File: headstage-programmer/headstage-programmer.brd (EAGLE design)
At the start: 22 x 49 mm, 19 parts, among them U1 TPS61202

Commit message: Minor change to headstage-programmer.
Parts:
- moved TP1 3.50 mm to (7.25, 27.8)
- moved TP2 3.50 mm to (3.75, 27.8)
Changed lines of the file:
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@@
 <wire x1="5" y1="49" x2="0" y2="44" width="0" layer="20"/>
 <wire x1="0" y1="44" x2="0" y2="0" width="0" layer="20"/>
-<text x="8" y="28.5" size="1.27" layer="21" font="vector" ratio="17" align="center-right">VCOAX</text>
-<text x="2.25" y="26.75" size="1.27" layer="21" font="vector" ratio="17" rot="R180" align="center-right">GND</text>
-<wire x1="3.75" y1="25.75" x2="3.75" y2="25.25" width="0.254" layer="21"/>
-<wire x1="7.25" y1="26.25" x2="6.75" y2="27.5" width="0.254" layer="21"/>
+<text x="7.25" y="26.75" size="1.27" layer="21" font="vector" ratio="17" rot="R90" align="center-right">VCOAX</text>
+<text x="3.75" y="26.75" size="1.27" layer="21" font="vector" ratio="17" rot="R90" align="center-right">GND</text>
 <wire x1="18.75" y1="18" x2="14" y2="18" width="0.254" layer="21"/>
-<wire x1="7.25" y1="26.25" x2="7.25" y2="25.5" width="0.254" layer="21"/>
 <text x="2" y="17.25" size="1.27" layer="21" font="vector" ratio="17" rot="R270" align="center-right">2.2uH</text>
 <wire x1="5" y1="45" x2="7.75" y2="46.75" width="0.254" layer="21"/>
@@
 <attribute name="VALUE" x="10.96" y="44.71" size="1.016" layer="27" font="vector" ratio="18"/>
 </element>
-<element name="TP1" library="jonnew" package="TESTPOINT_1MM" value="" x="7.25" y="24.25" smashed="yes">
-<attribute name="VALUE" x="8.266" y="23.7674" size="0.8128" layer="27" font="vector" ratio="18"/>
-</element>
-<element name="TP2" library="jonnew" package="TESTPOINT_1MM" value="" x="3.75" y="24.25" smashed="yes">
-<attribute name="VALUE" x="4.766" y="23.7674" size="0.8128" layer="27" font="vector" ratio="18"/>
+<element name="TP1" library="jonnew" package="TESTPOINT_1MM" value="" x="7.25" y="27.75" smashed="yes">
+<attribute name="VALUE" x="8.266" y="27.2674" size="0.8128" layer="27" font="vector" ratio="18"/>
+</element>
+<element name="TP2" library="jonnew" package="TESTPOINT_1MM" value="" x="3.75" y="27.75" smashed="yes">
+<attribute name="VALUE" x="4.766" y="27.2674" size="0.8128" layer="27" font="vector" ratio="18"/>
 </element>
 <element name="R1" library="jonnew" package="0603" value="2k" x="1.75" y="42" smashed="yes" rot="R270">

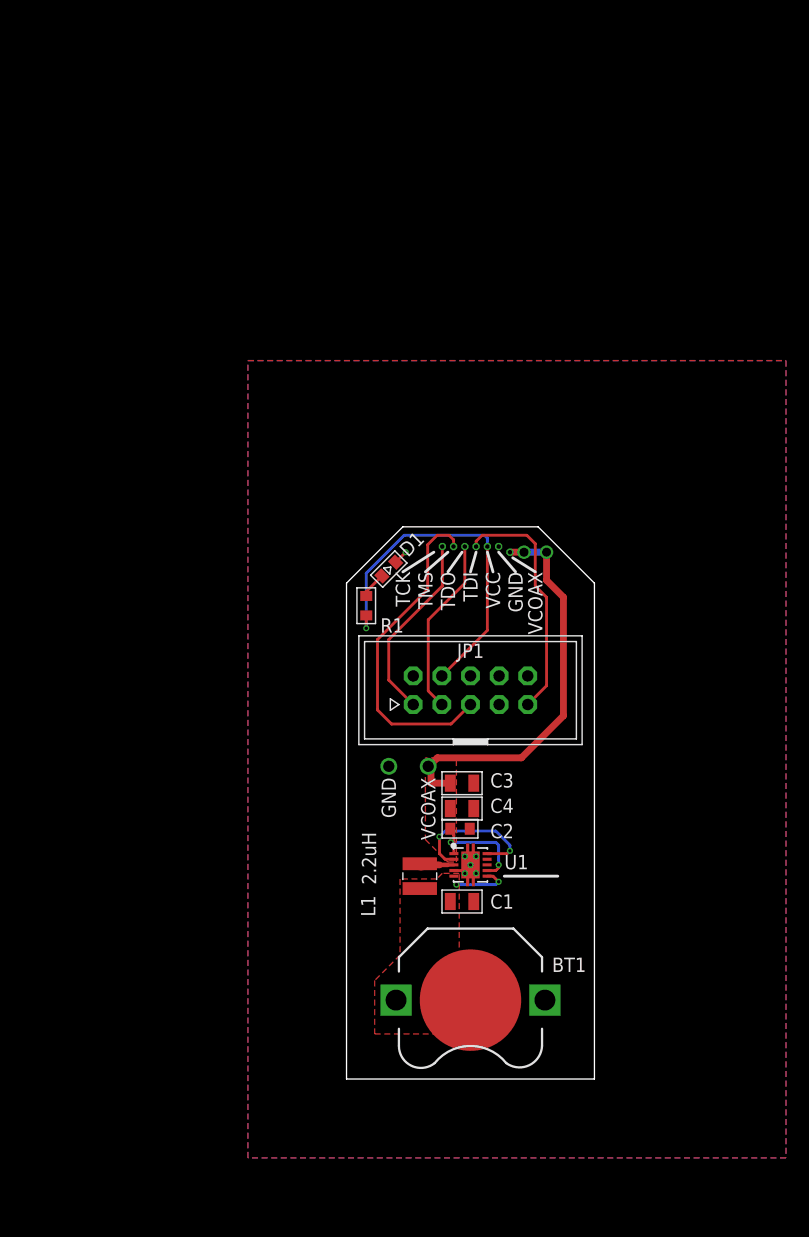
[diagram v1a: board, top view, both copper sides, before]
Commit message: Headstage programmer modifications
- Due to discussions with Jakob
- Coin cell replaced with AAA battery
- Orientation of programming pins rotated
- JTAG connector removed to rear
- Reverse polarity protection in case coax is plugged in during
programming
- Power switch
- Flashlight LED on bottom
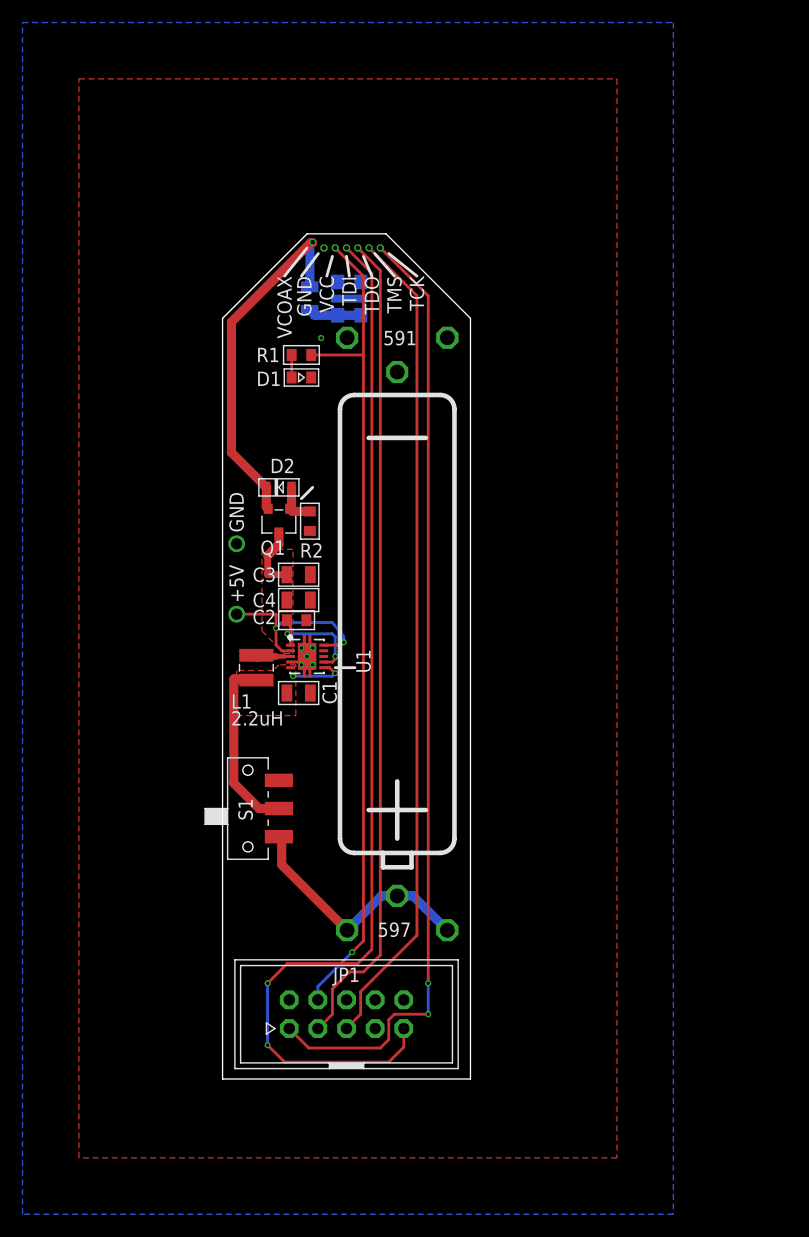
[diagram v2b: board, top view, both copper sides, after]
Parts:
- removed BT1: (no value), SparkFun-Batteries:BATTCON_12MM_PTH
- added D2: UDZ10B-7, jonnew:SOD-323
- added D3: MLEAWT-A1, jonnew:LED-MLE
- added Q1: DMP3056L, jonnew:SOT23-GSD
- added R2: 1k, jonnew:0603
- added R3: 220, jonnew:0805
- added S1: (no value), jonnew:JS102011SAQN
- added U2: (no value), jonnew:597/591_AAA-HOLDER
- moved VCOAX 32.6 mm to (-3.00, 74.2), turned to 180 degrees
- moved JP1 30.8 mm to (0.00, 5.75)
- moved GND 30.7 mm to (-2.00, 73.8), turned to 180 degrees
- moved VCC 29.7 mm to (-1.00, 73.8), turned to 180 degrees
- moved TDI 28.9 mm to (0.00, 73.8), turned to 180 degrees
- moved TDO 28.2 mm to (1.00, 73.8), turned to 180 degrees
- moved TMS 27.5 mm to (2.00, 73.8), turned to 180 degrees
- moved TCK 27.1 mm to (3.00, 73.8), turned to 180 degrees
- moved TP2 23.9 mm to (-9.75, 47.5)
- moved C1 23.5 mm to (-4.25, 34.2)
- moved C2 23.5 mm to (-4.43, 40.7)
- moved C3 23.5 mm to (-4.25, 44.8)
- moved C4 23.5 mm to (-4.25, 42.5)
- moved L1 23.5 mm to (-8.00, 36.5)
- moved U1 23.5 mm to (-3.50, 37.5)
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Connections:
- new net N$2: D3.A1, D3.A2, R3.1
- new net N$4: S1.3, U2.+1, U2.+2, U2.+3
- new net N$450: D2.A, Q1.G, R2.2
- new net VO: C3.1, C4.1, Q1.D, TP1.1, U1.10, U1.2
- net GND: now also D3.C1, D3.C2, D3.HS, R2.1, U2.-1, U2.-2, U2.-3; no longer BT1.GND
- net VCOAX: now also D2.C, Q1.S, R3.2; no longer C3.1, C4.1, TP1.1, U1.10, U1.2
- net VIN: now also S1.2; no longer BT1.VCC@1
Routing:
- net TDI: track 21.6 -> 94.1 mm, vias 0 -> 2
- net TCK: track 16.9 -> 85.1 mm, vias 0 -> 2
- net TDO: track 15.9 -> 73.1 mm
- net TMS: track 29.4 -> 73.6 mm
- net VCC(TRGT): track 32.2 -> 74.1 mm
- net VO: track 0.00 -> 22.8 mm, vias 0 -> 2
- net N$4: track 0.00 -> 22.4 mm
- net VIN: track 5.09 -> 21.4 mm
- net VCOAX: track 47.9 -> 32.3 mm, vias 4 -> 0
- net N$2: track 0.00 -> 4.70 mm
- net N$450: track 0.00 -> 3.87 mm
- net GND: track 2.34 -> 1.08 mm
- added copper zone on layer 1, net VO
- removed copper zone on layer 1, net VCOAX
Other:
- board size 22 x 49 mm -> 22 x 75 mm
- board text added: "+5V"
- board text added: "591"
- board text added: "597"
- board text removed: "VCOAX"

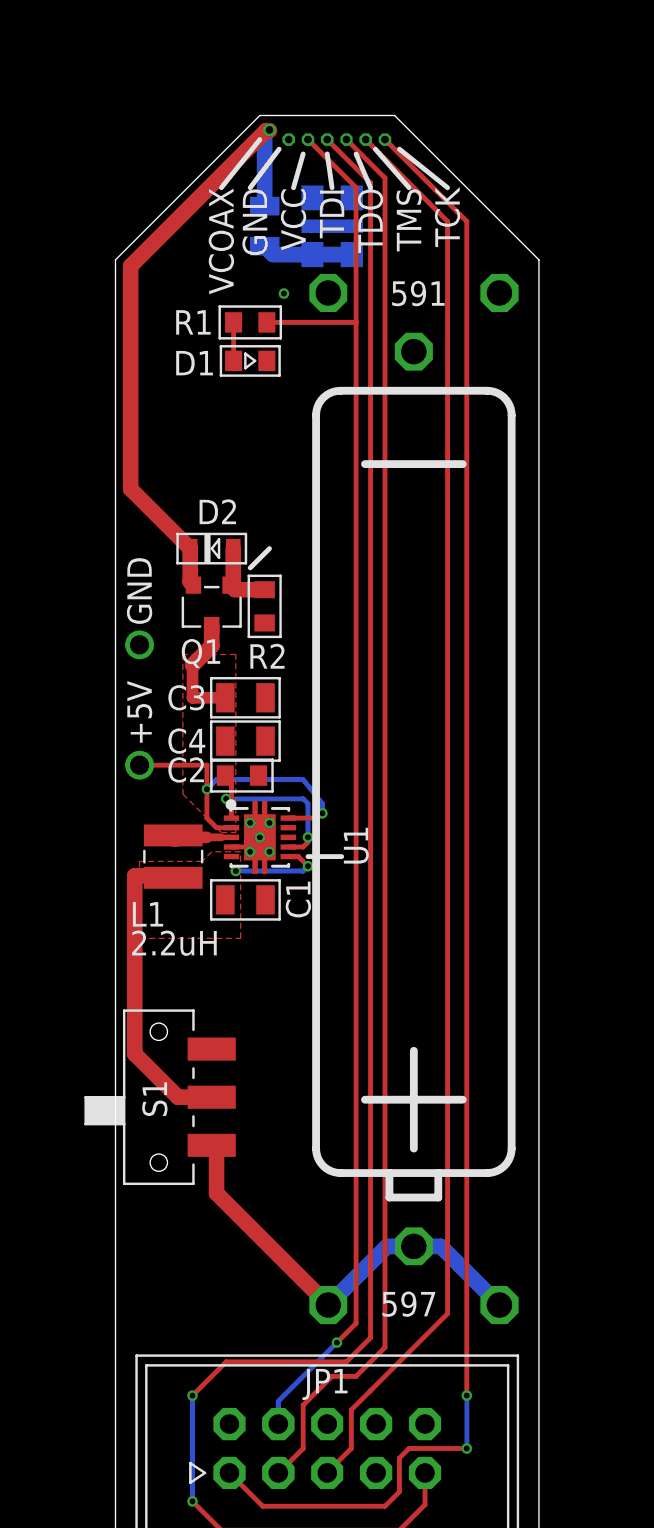
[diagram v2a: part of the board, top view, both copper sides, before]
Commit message: Changes to pogo JTAG programming dimensions
- Pins are now separated by 0.05 inches so that standard pins might be
possible to use
- There is not much clearance on the headstage-64 so we may still have
to use tiny pogo pins
- Fixed JTAG connectivity on headstage-64 by connecting +3V3 to
VCC(TRGT) pad
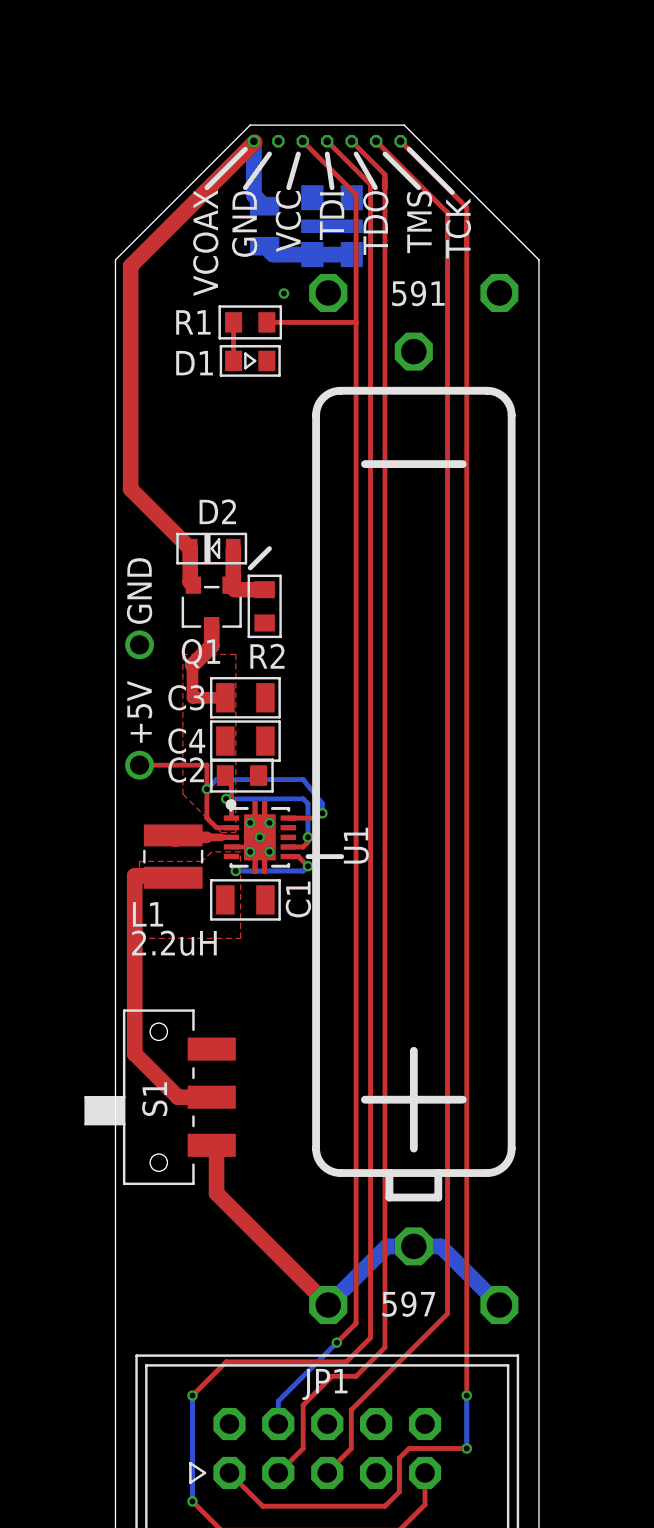
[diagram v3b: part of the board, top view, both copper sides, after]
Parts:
- moved VCOAX 1.00 mm to (-3.81, 73.7)
- moved TCK 0.81 mm to (3.81, 73.7)
- moved GND 0.55 mm to (-2.54, 73.7)
- moved TMS 0.55 mm to (2.54, 73.7)
- moved TDO 0.28 mm to (1.27, 73.7)
- moved VCC 0.28 mm to (-1.27, 73.7)
- moved TDI 0.09 mm to (0.00, 73.7)
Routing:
- net VCOAX: track 32.3 -> 30.7 mm
- net TCK: track 85.1 -> 85.9 mm
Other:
- board size 22 x 75 mm -> 22 x 74.5 mm

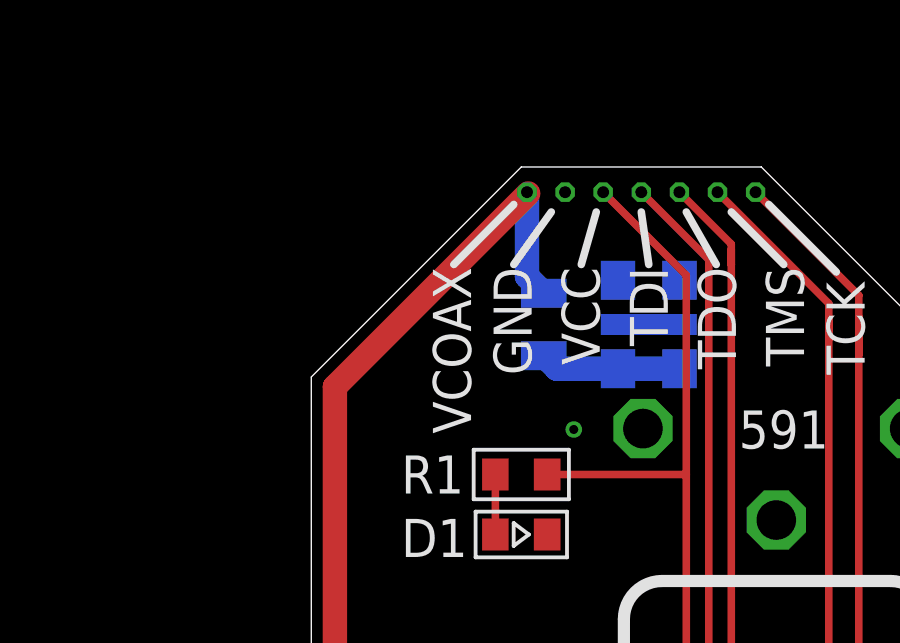
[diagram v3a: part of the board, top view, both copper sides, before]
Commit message: Headstage-64 routing refinements
- Update programmer to reflect switchee Vcoax/Gnd positions
- AGND/GND sprinkles for thermal and noise considerations
- Route optimization/simplificiation
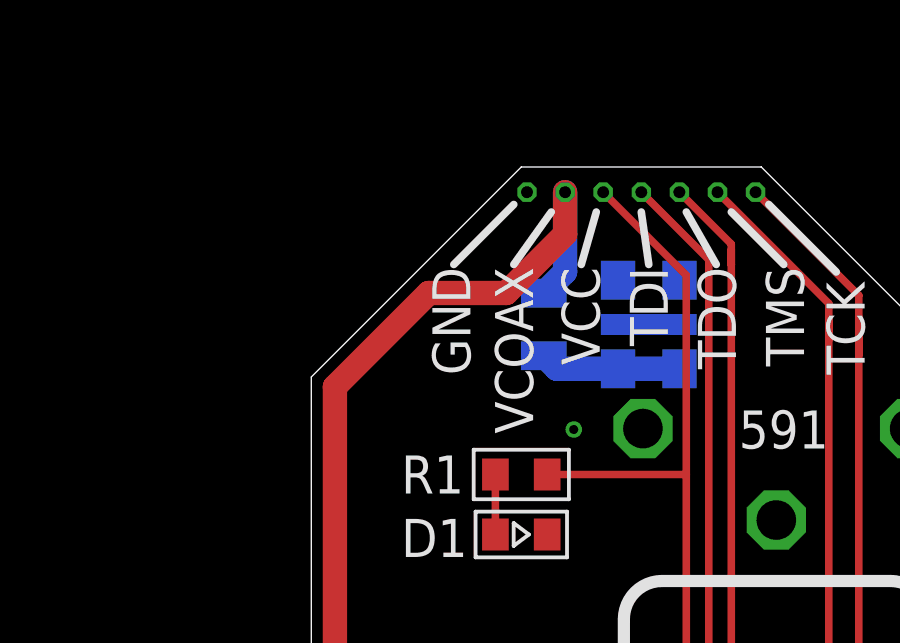
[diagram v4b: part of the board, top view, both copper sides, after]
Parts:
- moved GND 1.27 mm to (-3.81, 73.7)
- moved VCOAX 1.27 mm to (-2.54, 73.7)
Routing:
- net VCOAX: track 30.7 -> 32.8 mm
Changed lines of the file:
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@@
 <setting verticaltext="up"/>
 </settings>
-<grid distance="0.25" unitdist="mm" unit="mm" style="lines" multiple="1" display="yes" altdistance="5" altunitdist="mil" altunit="mil"/>
+<grid distance="0.1" unitdist="mm" unit="mm" style="lines" multiple="1" display="yes" altdistance="5" altunitdist="mil" altunit="mil"/>
 <layers>
 <layer number="1" name="Top" color="4" fill="1" visible="yes" active="yes"/>
@@
 <attribute name="VALUE" x="3.81" y="76.2" size="1.016" layer="27" font="vector" ratio="18" rot="R180"/>
 </element>
-<element name="VCOAX" library="jonnew" package="POGO_S500-6350-P2" value="" x="-3.81" y="73.66" smashed="yes" rot="R180">
-<attribute name="NAME" x="-6.31" y="71.16" size="1.27" layer="25" font="vector" ratio="17" rot="R270" align="center-left"/>
-<attribute name="VALUE" x="-1.27" y="76.2" size="1.016" layer="27" font="vector" ratio="18" rot="R180"/>
+<element name="VCOAX" library="jonnew" package="POGO_S500-6350-P2" value="" x="-2.54" y="73.66" smashed="yes" rot="R180">
+<attribute name="NAME" x="-4.24" y="71.16" size="1.27" layer="25" font="vector" ratio="17" rot="R270" align="center-left"/>
+<attribute name="VALUE" x="0" y="76.2" size="1.016" layer="27" font="vector" ratio="18" rot="R180"/>
 </element>
 <element name="TMS" library="jonnew" package="POGO_S500-6350-P2" value="" x="2.54" y="73.66" smashed="yes" rot="R180">
@@
 <attribute name="VALUE" x="-6.25" y="39.5" size="1.27" layer="27" font="vector" ratio="17" rot="R180" align="center-left"/>
 </element>
-<element name="GND" library="jonnew" package="POGO_S500-6350-P2" value="" x="-2.54" y="73.66" smashed="yes" rot="R180">
-<attribute name="NAME" x="-4.29" y="71.16" size="1.27" layer="25" font="vector" ratio="17" rot="R270" align="center-left"/>
-<attribute name="VALUE" x="0" y="76.2" size="1.016" layer="27" font="vector" ratio="18" rot="R180"/>
+<element name="GND" library="jonnew" package="POGO_S500-6350-P2" value="" x="-3.81" y="73.66" smashed="yes" rot="R180">
+<attribute name="NAME" x="-6.33" y="71.16" size="1.27" layer="25" font="vector" ratio="17" rot="R270" align="center-left"/>
+<attribute name="VALUE" x="-1.27" y="76.2" size="1.016" layer="27" font="vector" ratio="18" rot="R180"/>
 </element>
 <element name="TP1" library="jonnew" package="TESTPOINT_1MM" value="" x="-9.75" y="41.25" smashed="yes">
@@
 <wire x1="-7.1176" y1="52.5" x2="-10.2126" y2="55.595" width="0.8128" layer="1"/>
 <wire x1="-10.2126" y1="55.595" x2="-10.2126" y2="67.17384375" width="0.8128" layer="1"/>
-<wire x1="-3.768221875" y1="73.618221875" x2="-10.2126" y2="67.17384375" width="0.8128" layer="1"/>
-<wire x1="-3.25" y1="70.2914" x2="-3.81" y2="70.8514" width="0.8128" layer="16"/>
-<wire x1="-3.81" y1="73.57644375" x2="-3.81" y2="70.8514" width="0.8128" layer="16"/>
-<wire x1="-3.81" y1="73.66" x2="-3.768221875" y2="73.618221875" width="0.254" layer="1"/>
-<wire x1="-3.81" y1="73.66" x2="-3.81" y2="73.57644375" width="0.254" layer="16"/>
+<wire x1="-10.2126" y1="67.17384375" x2="-7.08644375" y2="70.3" width="0.8128" layer="1"/>
+<wire x1="-2.54" y1="72.26" x2="-2.54" y2="73.66" width="0.8128" layer="1"/>
+<wire x1="-7.08644375" y1="70.3" x2="-4.5" y2="70.3" width="0.8128" layer="1"/>
+<wire x1="-4.5" y1="70.3" x2="-2.54" y2="72.26" width="0.8128" layer="1"/>
+<wire x1="-3.25" y1="70.2914" x2="-2.54" y2="71.0014" width="0.8128" layer="16"/>
+<wire x1="-2.54" y1="71.0014" x2="-2.54" y2="73.66" width="0.8128" layer="16"/>
 </signal>
 <signal name="N$2">
